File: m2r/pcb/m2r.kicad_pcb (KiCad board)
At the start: 2 copper layers, 50 x 75 mm, 118 parts, among them IC1 ADP3338, IC10 STM32F303C, IC11 ADP3333, IC2 ADP3335, IC3 ADuM1201, IC4 ADuM1201, IC5 ADuM1201, IC6 MTX2, IC7 ADL5324, IC8 MAX-7Q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

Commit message: shipping
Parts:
- moved G*** 0.90 mm to (161.5, 87.5)
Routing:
- net GND: track 290.9 -> 391.1 mm, vias 85 -> 136
- net Net-(D9-Pad1): track 5.50 -> 40.2 mm
- net Net-(GS1-Pad1): track 31.3 -> 38.5 mm
- net +3.3V: track 199.8 -> 204.4 mm
- net Net-(ANT1-Pad1): track 3.79 -> 7.57 mm
- net +5V: track 67.2 -> 66.5 mm
- added copper zone on F.Cu, net +5V
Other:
- board text added: "ADAM GREIG 2014-07-23"
- board text added: "r1"
- board text removed: "R1 ADAM GREIG 2014-07-23"

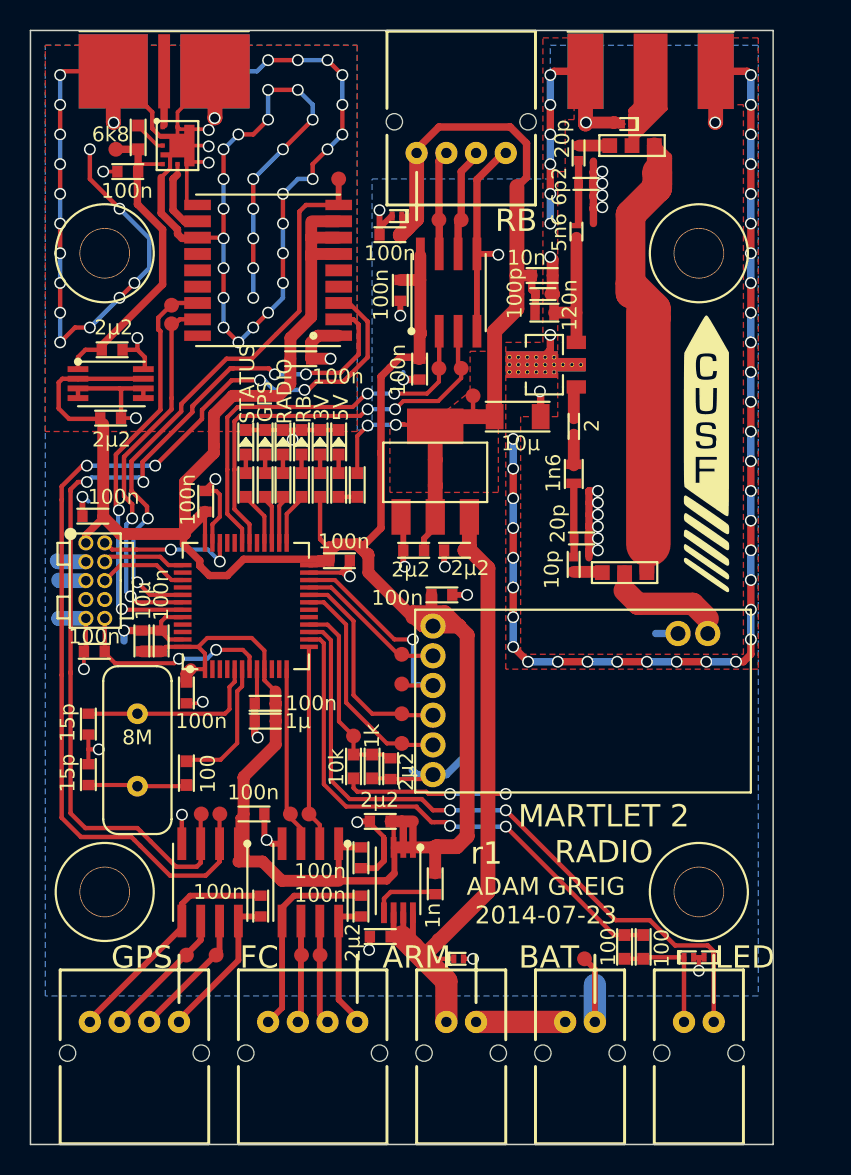
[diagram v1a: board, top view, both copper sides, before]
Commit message: changed ESD diode to 12V one
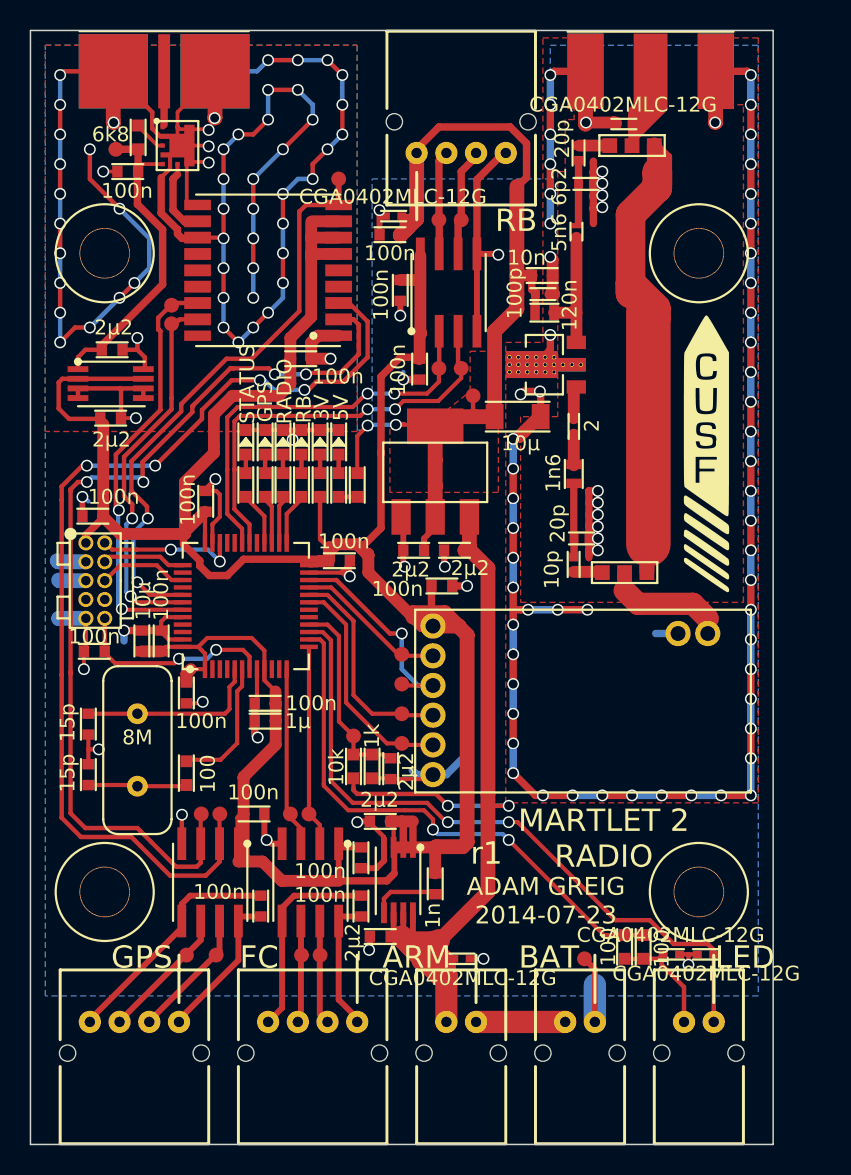
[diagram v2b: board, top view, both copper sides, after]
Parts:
- D10, D11, D7, D8, D9: value ESD5V3S1U -> CGA0402MLC-12G; footprint m2r:TSLP-2-17 -> m2r:R0402
- moved D10 2.31 mm to (159.7, 121.2)
- moved D11 0.92 mm to (160.9, 121.2)
- moved C15 0.60 mm to (143.0, 96.4)
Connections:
- D10 pad 1: LED_C -> GND
- D10 pad 2: GND -> Net-(D10-Pad2)
- D11 pad 1: Net-(D11-Pad1) -> GND
- D11 pad 2: GND -> LED_C
- P8 pad 2: Net-(D11-Pad1) -> Net-(D10-Pad2)
- R4 pad 1: Net-(D11-Pad1) -> Net-(D10-Pad2)
- R5 pad 1: Net-(D11-Pad1) -> Net-(D10-Pad2)
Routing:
- net GND: track 391.1 -> 419.4 mm, vias 136 -> 148
- net +BATT: track 62.7 -> 76.7 mm
- net Net-(D11-Pad1): track 8.72 -> 0.00 mm
- net Net-(D10-Pad2): track 0.00 -> 8.41 mm
- net +3.3V: track 204.4 -> 205.7 mm
- net LED_A: track 36.8 -> 37.4 mm

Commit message: further tweaks
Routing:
- net GND: track 419.4 -> 422.1 mm, vias 148 -> 150

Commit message: done pls
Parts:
- moved TP18 10.2 mm to (123.9, 77.0)
- moved IC11 4.57 mm to (123.2, 79.6), turned to 270 degrees
- moved C31 4.48 mm to (127.7, 68.0), turned to 90 degrees
- moved C32 3.92 mm to (123.9, 78.1), turned to 180 degrees
- moved R6 3.32 mm to (126.4, 68.0)
- moved IC9 2.58 mm to (125.2, 65.5), turned to 270 degrees
- moved TP20 2.15 mm to (126.4, 80.7)
- moved C33 1.82 mm to (122.5, 85.4), turned to 180 degrees
- moved TP21 0.85 mm to (125.2, 76.7)
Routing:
- net Net-(C31-Pad1): track 21.9 -> 37.2 mm, vias 0 -> 2
- net GND: track 422.1 -> 432.5 mm, vias 150 -> 156
- net +3.3V: track 205.7 -> 201.1 mm
- net Net-(ANT1-Pad1): track 7.57 -> 4.19 mm
- net Net-(IC8-Pad11): track 5.40 -> 6.30 mm
- net GPS_SDA: track 28.4 -> 29.3 mm
- net GPS_RESET: track 39.9 -> 40.6 mm
- net Net-(IC9-Pad11): track 2.27 -> 1.62 mm
- net GPS_SCL: track 25.7 -> 26.4 mm

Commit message: change alm silk, bottom mask on sma, add better gnd track to rb
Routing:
- net GND: track 432.5 -> 427.3 mm
